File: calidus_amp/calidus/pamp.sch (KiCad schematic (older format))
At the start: 56 parts, among them U4 TDA7293, U5 TDA7293

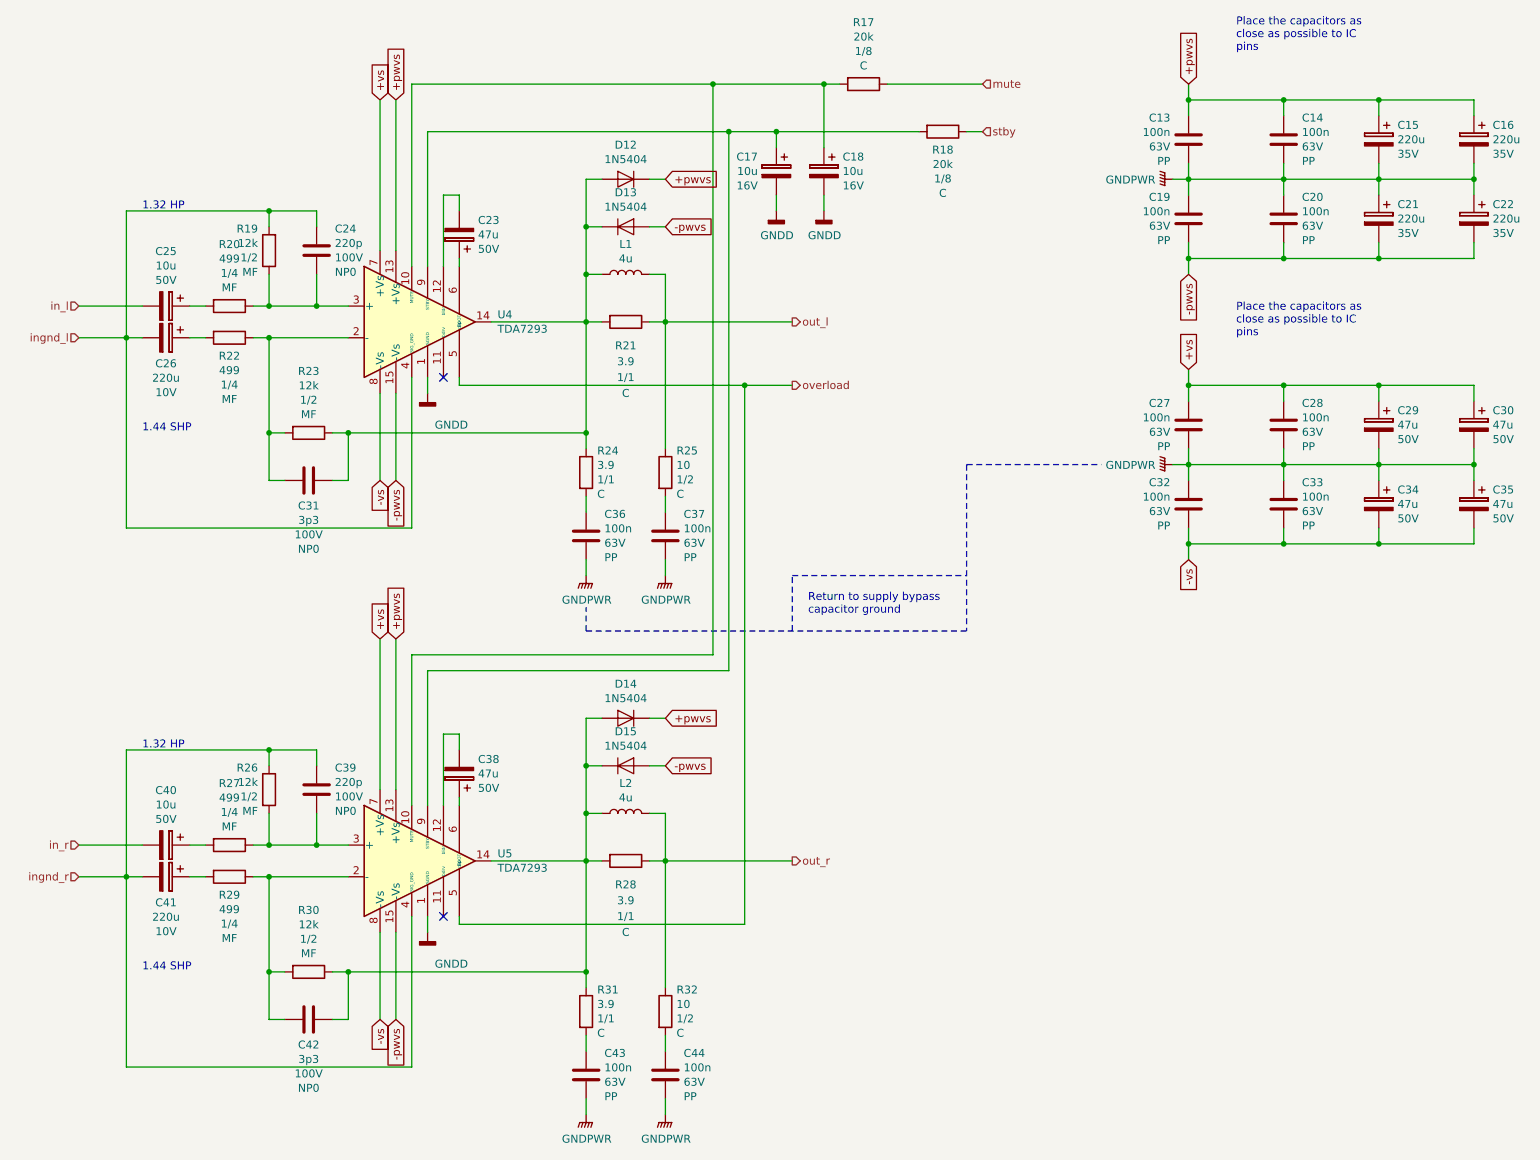
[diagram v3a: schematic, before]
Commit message: WIP: Component placement and footprint assignement
- Finished all capacitors
- Finished all ICs
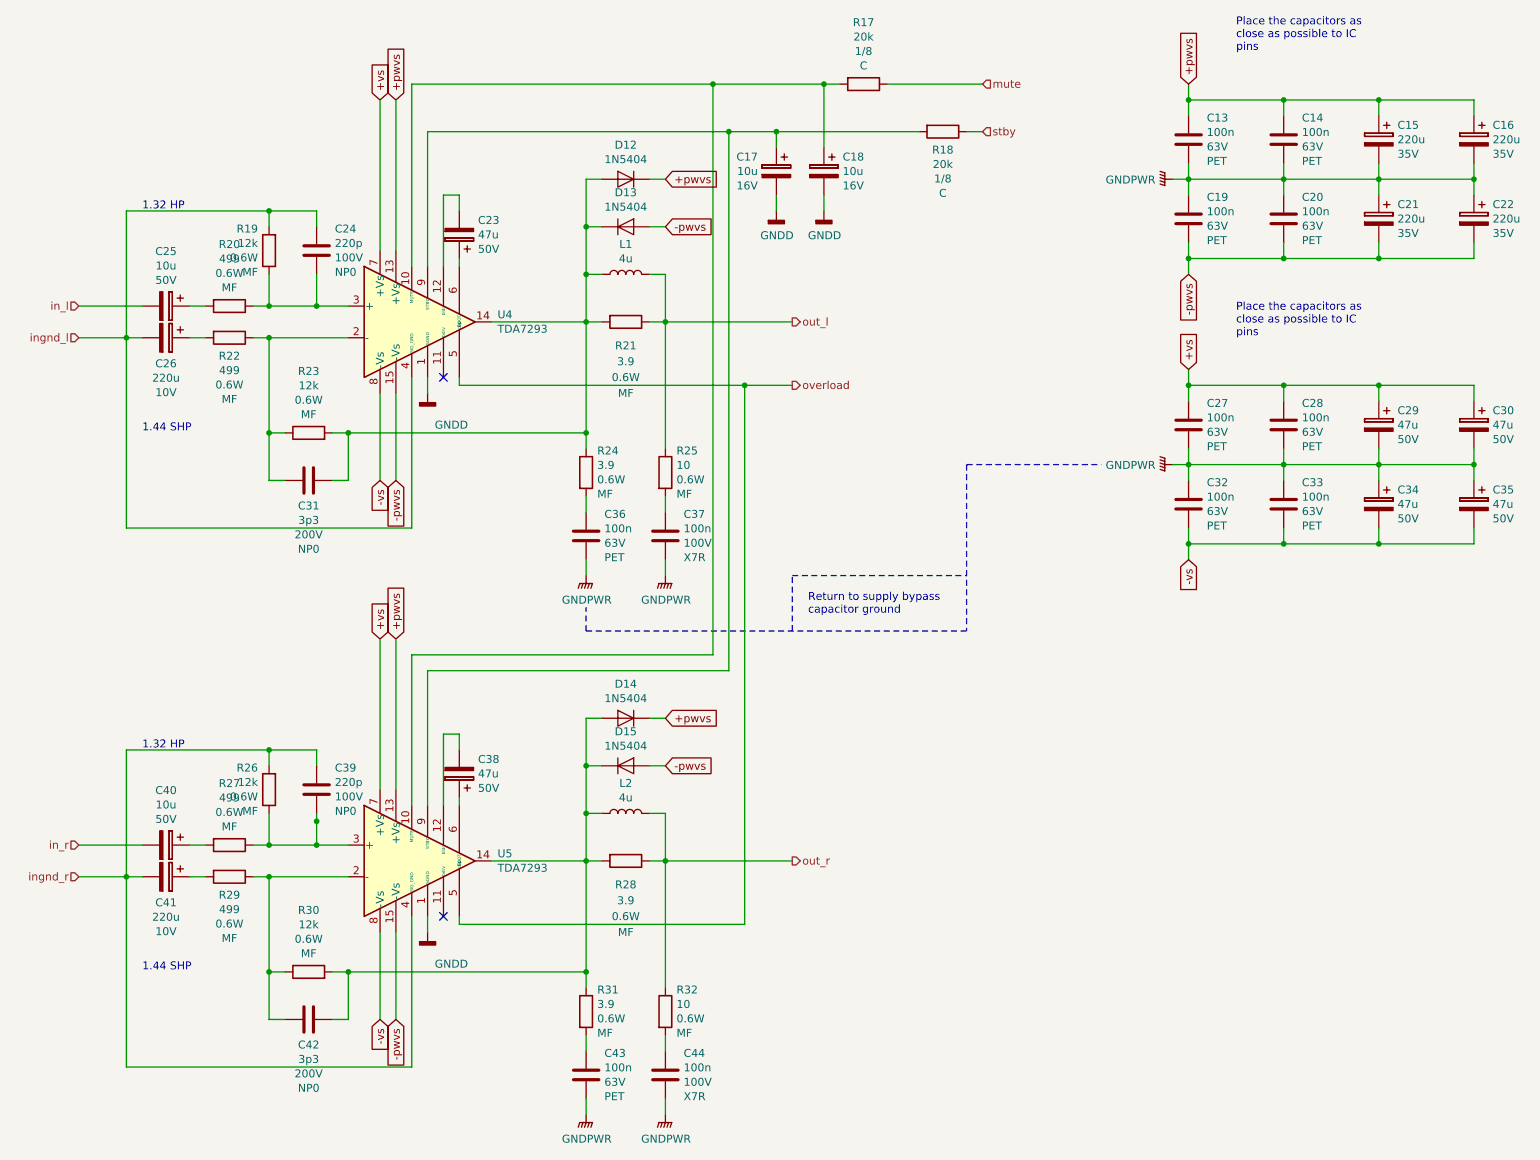
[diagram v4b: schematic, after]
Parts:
- C13, C14, C19, C20, C27, C28, C32, C33, C36, C43: footprint Capacitor_THT:C_Rect_L7.0mm_W2.5mm_P5.00mm -> Capacitor_THT:C_Rect_L4.6mm_W3.0mm_P2.50mm_MKS02_FKP02; Manufacturer (none) -> WIMA:MKS0C031000C00KSSD; Supplier1 (none) -> Farnell:1006004; Type PP -> PET
- C24, C39: footprint Capacitor_THT:C_Disc_D3.0mm_W1.6mm_P2.50mm -> Capacitor_THT:C_Disc_D3.8mm_W2.6mm_P2.50mm; Manufacturer (none) -> AVX:SR151A221JAR; Supplier1 (none) -> Farnell:1100374
- C31, C42: footprint Capacitor_THT:C_Disc_D3.0mm_W1.6mm_P2.50mm -> Capacitor_THT:C_Disc_D3.8mm_W2.6mm_P2.50mm; Manufacturer (none) -> Kemet:C315C339D2G5TA; Supplier1 (none) -> Farnell:2819636; Voltage 100V -> 200V
- C37, C44: footprint Capacitor_THT:C_Rect_L7.0mm_W2.5mm_P5.00mm -> Capacitor_THT:C_Disc_D5.1mm_W3.2mm_P5.00mm; Manufacturer (none) -> AVX:SR211C104KAR; Supplier1 (none) -> Farnell:1006004; Type PP -> X7R; Voltage 63V -> 100V
- R19, R23, R26, R30: Manufacturer (none) -> TE Connectivity:LR1F12K; Power 1/2 -> 0.6W; Supplier1 (none) -> Farnell:2330007
- R20, R22, R27, R29: Manufacturer (none) -> TE Connectivity:LR1F499R; Power 1/4 -> 0.6W; Supplier1 (none) -> Farnell:2330163
- R21, R24, R28, R31: Manufacturer (none) -> TE Connectivity:LR1F3R9; Power 1/1 -> 0.6W; Supplier1 (none) -> Farnell:2330141; Type C -> MF
- R25, R32: Manufacturer (none) -> TE Connectivity:LR1F10R; Power 1/2 -> 0.6W; Supplier1 (none) -> Farnell:2329993; Type C -> MF
- U4, U5: Manufacturer (none) -> ST:TDA7293V; Supplier1 (none) -> Farnell:1366582
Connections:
- net ingnd_r: now also R26.2; no longer R26.1
- net at C31.1, D12.2 (A), D13.1 (K)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: now also R23.2; no longer R23.1
- net at C31.2, R22.1, U4.2 (-): now also R23.1; no longer R23.2
- net at C42.1, D14.2 (A), D15.1 (K)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: now also R30.2; no longer R30.1
- net at C42.2, R29.1, U5.2 (-): now also R30.1; no longer R30.2
- net at C39.1, R27.1, U5.3 (+): now also R26.1; no longer R26.2
